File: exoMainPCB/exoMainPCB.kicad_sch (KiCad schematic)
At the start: 76 parts, among them J1 Conn_02x06_Odd_Even, J10 Conn_01x03_Pin, J11 USB_A, J12 USB_A, J13 USB_A, J2 HDMI_A, J3 USB_A, J6 Conn_01x03_Pin, SW3 SW_SPDT, SW4 SW_SPDT, U1 MCP2515-I/ST, U14 SI8642ED-B-IS, U15 SN65HVD230D, U16 SN65HVD230D, U17 SM24CANB-02HTG, U18 SM24CANB-02HTG, U2 MCP2515-I/ST, U3 BNO085, U4 SL2.1A, U5 MCP3008, Y1 16 MHz, Y2 16 MHz, Y3 12 MHz, Y4 32.768 kHz

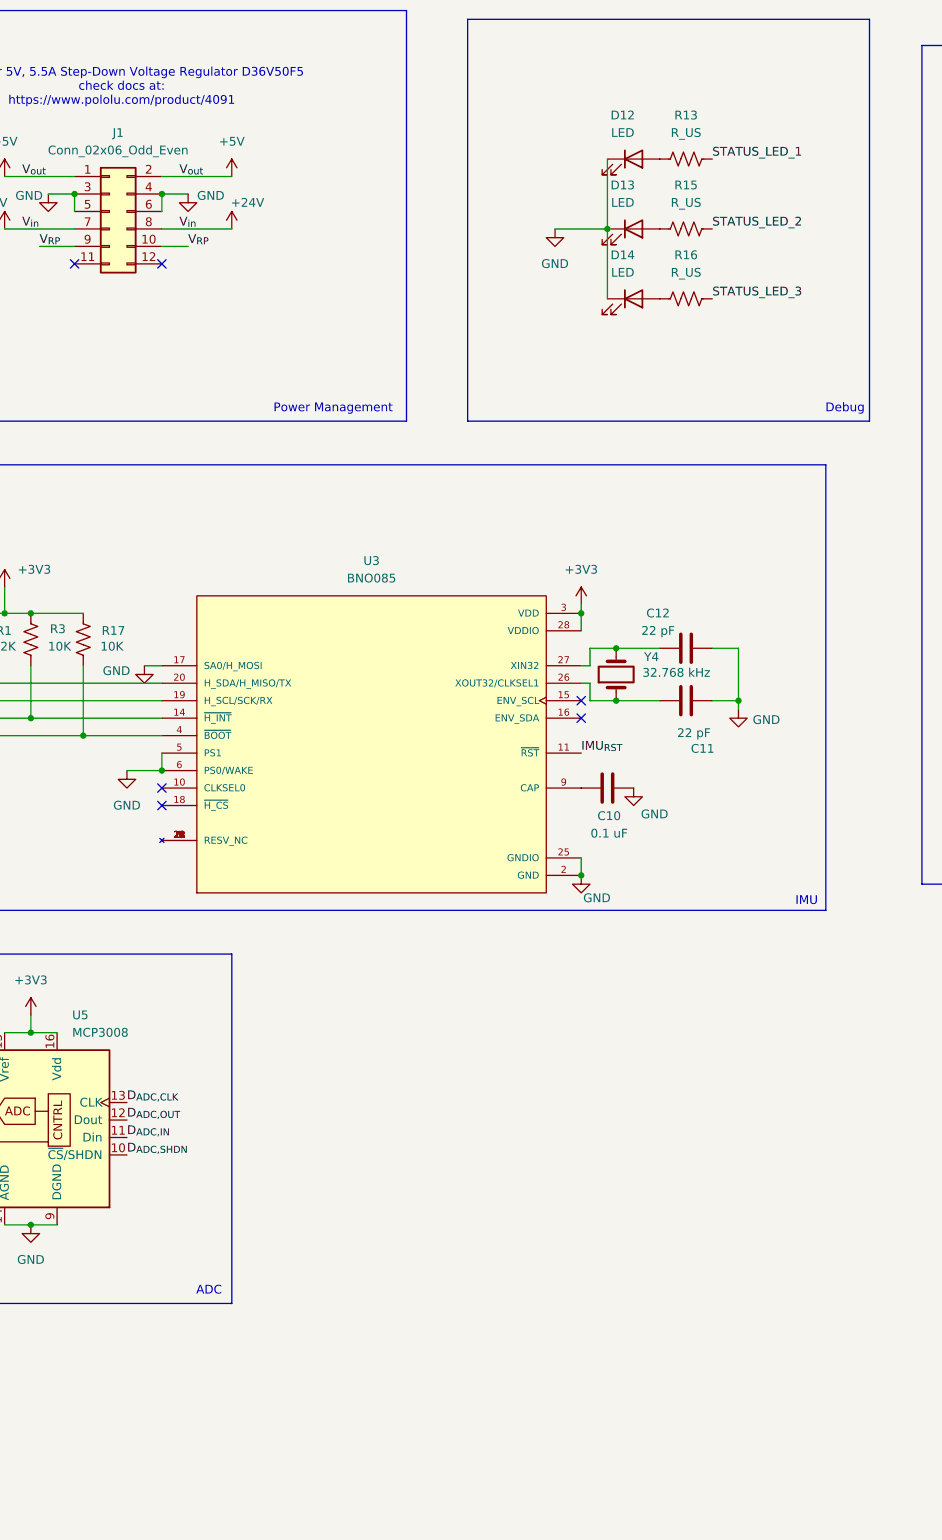
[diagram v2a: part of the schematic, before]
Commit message: added headers to connect to sensors + terminals for battery
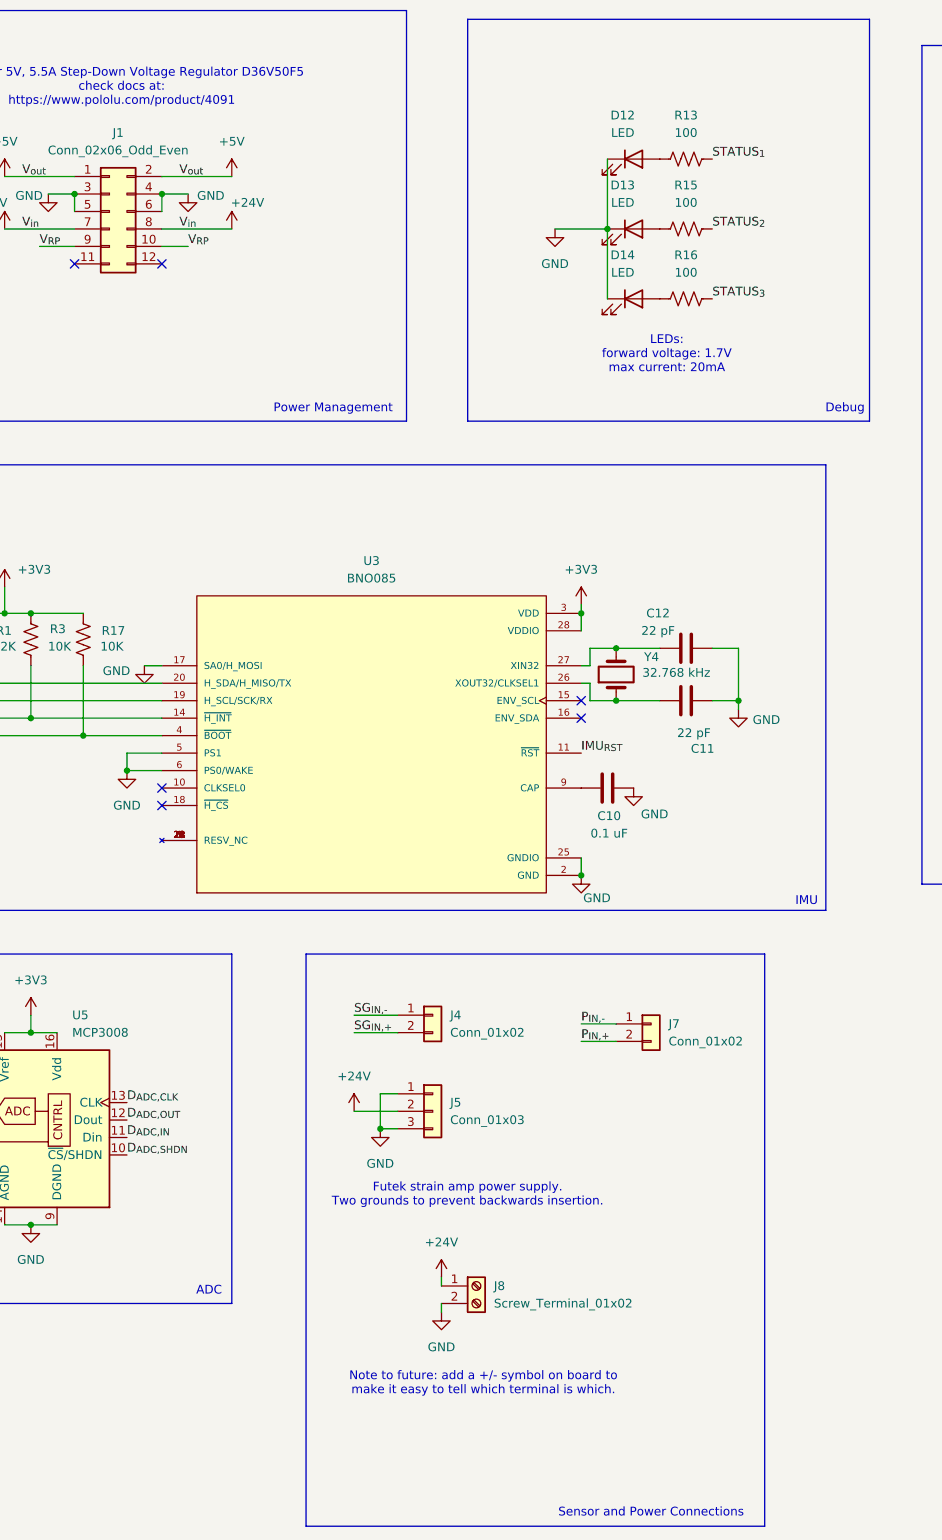
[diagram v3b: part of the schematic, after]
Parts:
- added J4, J7: Conn_01x02, symbol Connector_Generic:Conn_01x02
- added J5: Conn_01x03, symbol Connector_Generic:Conn_01x03
- added J8: Screw_Terminal_01x02, symbol Connector:Screw_Terminal_01x02
- D12, D13, D14: footprint (none) -> LED_SMD:LED_1206_3216Metric
- R13, R15, R16: value R_US -> 100
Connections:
- net +24V: now also J5.2 (Pin_2), J8.1 (Pin_1)
- net GND: now also J5.1 (Pin_1), J5.3 (Pin_3), J8.2 (Pin_2)
- net P_{IN,+}: now also J7.2 (Pin_2)
- net P_{IN,-}: now also J7.1 (Pin_1)
- net SG_{IN,+}: now also J4.2 (Pin_2)
- net SG_{IN,-}: now also J4.1 (Pin_1)
- net STATUS_LED_1 renamed STATUS_{1}
- net STATUS_LED_2 renamed STATUS_{2}
- net STATUS_LED_3 renamed STATUS_{3}
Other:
- note added: "Futek strain amp power supply. Two grounds to prevent backwards insertion."
- note added: "LEDs: forward voltage: 1.7V max current: 20mA"
- note added: "Note to future: add a +/- symbol on board to make it easy to tell which terminal is which."
- note added: "Sensor and Power Connections"

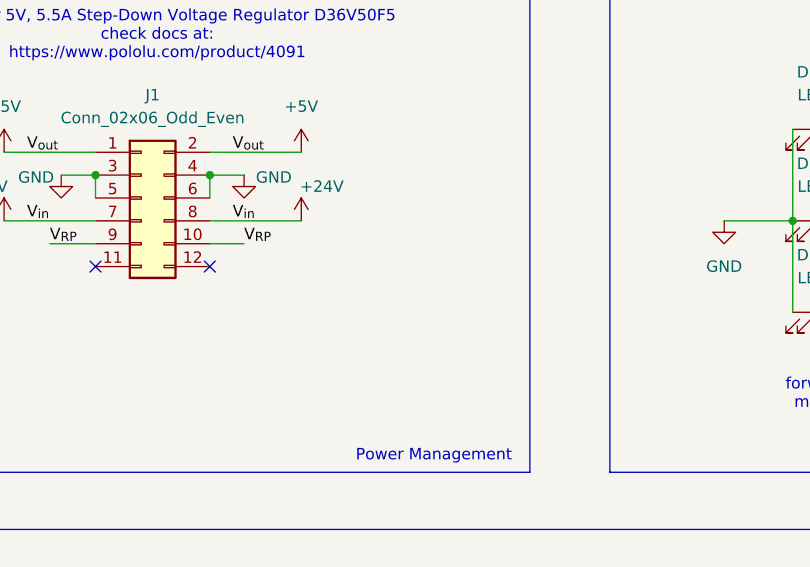
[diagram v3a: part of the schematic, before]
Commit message: added power indicator LED
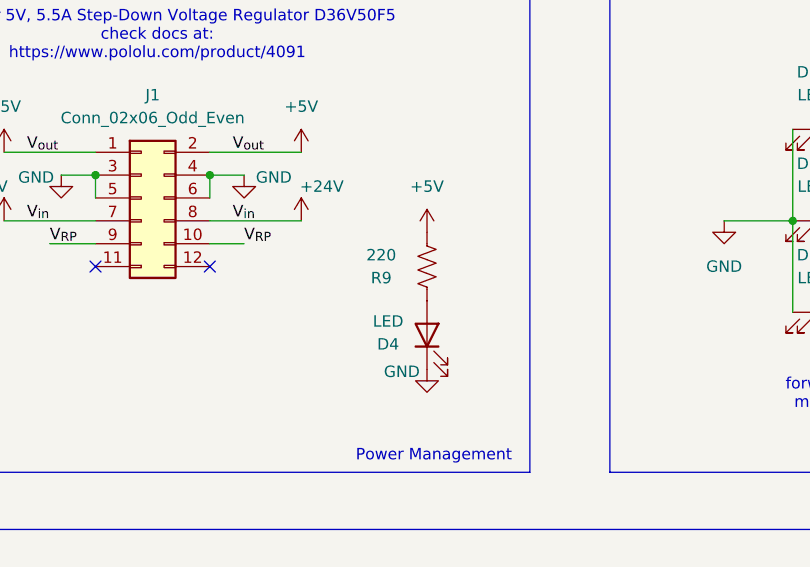
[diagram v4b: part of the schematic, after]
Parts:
- added D4: LED, LED_SMD:LED_1206_3216Metric, symbol Device:LED
- added R9: 220, symbol Device:R_US
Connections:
- net +5V: now also R9.2
- net GND: now also D4.1 (K)
- new net: D4.2 (A), R9.1
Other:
- company: (none) -> Stanford Biomechatronics Lab
- title: (none) -> Untethered Ankle Exoskeleton Control Board

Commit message: added external SD and connected all pins to CM5
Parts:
- added C18: 10uF, symbol Device:C
- added J15: Micro_SD_Card_Det2, symbol Connector:Micro_SD_Card_Det2
- added J9: Screw_Terminal_01x02, symbol Connector:Screw_Terminal_01x02
- added R12: 12K, symbol Device:R_US
- added U6: RT9742GGJ5, Package_TO_SOT_SMD:SOT-23-5, symbol CM5IO:RT9742GGJ5
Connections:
- net D_{ADC,CLK} is gone; now on net SCK: U5.13 (CLK)
- net D_{ADC,IN} is gone; now on net MOSI: U5.11 (Din)
- net D_{ADC,OUT} is gone; now on net MISO: U5.12 (Dout)
- net D_{ADC,SHDN} is gone; now on net D_{CS,ADC}: U5.10 (~{CS}/SHDN)
- net D_{SCK0} is gone; now on net SCK: U1.14 (SCK)
- net D_{SCK1} is gone; now on net SCK: U2.14 (SCK)
- net D_{SI0} is gone; now on net MOSI: U1.16 (SI)
- net D_{SI1} is gone; now on net MOSI: U2.16 (SI)
- net D_{SO0} is gone; now on net MISO: U1.17 (SO)
- net D_{SO1} is gone; now on net MISO: U2.17 (SO)
- net +24V: now also J9.1 (Pin_1)
- net +3V3: now also Module1.78 (GPIO_VREF(1.8v/3.3v_Input)), Module1.84 (+3.3v_(Output)), Module1.86 (+3.3v_(Output)), R12.1, U6.5 (IN)
- net +5V: now also Module1.77 (+5v_(Input)), Module1.79 (+5v_(Input)), Module1.81 (+5v_(Input)), Module1.83 (+5v_(Input)), Module1.85 (+5v_(Input)), Module1.87 (+5v_(Input))
- net D_{CS0}: now also Module1.24 (GPIO26)
- net D_{CS1}: now also Module1.26 (GPIO19)
- net D_{HDMI0_CLK_N}: now also Module1.190 (HDMI0_CLK_N)
- net D_{HDMI0_CLK_P}: now also Module1.188 (HDMI0_CLK_P)
- net D_{HDMI0_HOTPLUG}: now also Module1.153 (HDMI0_HOTPLUG)
- net D_{HDMI0_SCL}: now also Module1.200 (HDMI0_SCL)
- net D_{HDMI0_SDA}: now also Module1.199 (HDMI0_SDA)
- net D_{HDMI0_TX0_N}: now also Module1.184 (HDMI0_TX0_N)
- net D_{HDMI0_TX0_P}: now also Module1.182 (HDMI0_TX0_P)
- net D_{HDMI0_TX1_N}: now also Module1.178 (HDMI0_TX1_N)
- net D_{HDMI0_TX1_P}: now also Module1.176 (HDMI0_TX1_P)
- net D_{HDMI0_TX2_N}: now also Module1.172 (HDMI0_TX2_N)
- net D_{HDMI0_TX2_P}: now also Module1.170 (HDMI0_TX2_P)
- net D_{INT0}: now also Module1.28 (GPIO13)
- net D_{INT1}: now also Module1.30 (GPIO6)
- net D_{USB_N}: now also Module1.103 (USB2_N)
- net D_{USB_P}: now also Module1.105 (USB2_P)
- net GND: now also Module1.1 (GND), Module1.107 (GND), Module1.108 (GND), Module1.113 (GND), Module1.114 (GND), Module1.119 (GND), Module1.120 (GND), Module1.125 (GND), Module1.126 (GND), Module1.13 (GND), Module1.131 (GND), Module1.132 (GND), Module1.137 (GND), Module1.138 (GND), Module1.14 (GND), Module1.144 (GND), Module1.150 (GND), Module1.155 (GND), Module1.156 (GND), Module1.161 (GND), Module1.162 (GND), Module1.167 (GND), Module1.168 (GND), Module1.173 (GND), Module1.174 (GND), Module1.179 (GND), Module1.180 (GND), Module1.185 (GND), Module1.186 (GND), Module1.191 (GND), Module1.192 (GND), Module1.197 (GND), Module1.198 (GND), Module1.2 (GND), Module1.22 (GND), Module1.23 (GND), Module1.32 (GND), Module1.33 (GND), Module1.42 (GND), Module1.43 (GND), Module1.52 (GND), Module1.53 (GND), Module1.59 (GND), Module1.60 (GND), Module1.65 (GND), Module1.66 (GND), Module1.7 (GND), Module1.71 (GND), Module1.74 (GND), Module1.8 (GND), Module1.98 (GND), C18.2, J15.11 (SHIELD), J15.6 (VSS), J9.2 (Pin_2), U6.2 (GND)
- net IMU_{BOOT}: now also Module1.46 (GPIO22)
- net IMU_{HINT}: now also Module1.48 (GPIO27)
- net IMU_{RST}: now also Module1.50 (GPIO17)
- net SCL: now also Module1.56 (GPIO3)
- net SDA: now also Module1.58 (GPIO2)
- net STATUS_{1}: now also Module1.41 (GPIO25)
- net STATUS_{2}: now also Module1.39 (GPIO8)
- net STATUS_{3}: now also Module1.37 (GPIO7)
- net D_{CS,ADC}: now reaches Module1.34 (GPIO5)
- net SCK: now reaches Module1.38 (GPIO11)
- net MISO: now reaches Module1.40 (GPIO9)
- net MOSI: now reaches Module1.44 (GPIO10)
- net SD_{CLK}: now reaches Module1.57 (SD_CLK)
- net SD_{CLK}: now also J15.5 (CLK)
- net SD_{DAT,3}: now reaches Module1.61 (SD_DAT3)
- net SD_{DAT,3}: now also J15.2 (DAT3/CD)
- net SD_{CMD}: now reaches Module1.62 (SD_CMD)
- net SD_{CMD}: now also J15.3 (CMD)
- net SD_{DAT,0}: now reaches Module1.63 (SD_DAT0)
- net SD_{DAT,0}: now also J15.7 (DAT0)
- net SD_{DAT,1}: now reaches Module1.67 (SD_DAT1)
- net SD_{DAT,1}: now also J15.8 (DAT1)
- net SD_{DAT,2}: now reaches Module1.69 (SD_DAT2)
- net SD_{DAT,2}: now also J15.1 (DAT2)
- net SD_{PWRON}: now reaches Module1.75 (SD_PWR_ON)
- net SD_{PWRON}: now also R12.2, U6.4 (EN)
- new net SD_{PWR}: C18.1, J15.4 (VDD), U6.1 (OUT)
- no-connect marks 31 -> 32

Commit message: \added voltage inputs for the USB hub and CAN, down to 2 errors (can explain possible fix), 12 warnings (ignore the units warnings for the diode for now)
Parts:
- removed C34: 104, symbol Device:C
- removed R27: 120, symbol Device:R_US
- removed SW4: SW_SPDT, symbol Switch:SW_SPDT
- removed U16: SN65HVD230D, SOIC127P600X175-8N, symbol SN65HVD230:SN65HVD230D
- removed U18: SM24CANB-02HTG, SM24CANB02HTG, symbol SM24CANB:SM24CANB-02HTG
- added C19: 104, symbol Device:C
- added R14: 120, symbol Device:R_US
- added SW1: SW_SPDT, symbol Switch:SW_SPDT
- added U7: SN65HVD230D, SOIC127P600X175-8N, symbol SN65HVD230:SN65HVD230D
- added U8: SM24CANB-02HTG, SM24CANB02HTG, symbol SM24CANB:SM24CANB-02HTG
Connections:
- net +3V3: now also C16.2, C33.2, C5.2, C6.1, R4.1, R5.1, U1.20 (VDD), U14.1 (VDD1), U14.16 (VDD2), U15.3 (VCC), U2.20 (VDD), U4.13 (VDD33), C19.2, U7.3 (VCC)
- net D_{HDMI0_CEC}: now also Module1.151 (HDMI0_CEC)
- net GNDS: now also C33.1, R6.2, R7.2, C19.1, U7.2 (GND), U8.3; no longer C33.2, R6.1, R7.1
- net RXD_1B: now also U7.4 (R)
- net TXD_1B: now also U7.1 (D)
- net at J10.3 (Pin_3): now also R14.2, U7.7 (CANH), U8.1
- net +1V8: now reaches C15.2, U4.14 (VDD18)
- net +1V8: now also Module1.88 (+1.8v_(Output))
- net at J10.2 (Pin_2): now also SW1.1 (A), U7.6 (CANL), U8.2
- net at U15.8 (RS): now also R6.1; no longer R6.2
- new net: R7.1, U7.8 (RS)
- new net: R14.1, SW1.2 (B)
- no-connect marks 32 -> 143
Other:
- moved on the sheet: C33, C5, C6, R26, R6, SW3, U17

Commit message: removed sd card due to emmc, added battery voltage connection to ADC
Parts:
- removed C18: 10uF, symbol Device:C
- removed J15: Micro_SD_Card_Det2, symbol Connector:Micro_SD_Card_Det2
- removed U6: RT9742GGJ5, Package_TO_SOT_SMD:SOT-23-5, symbol CM5IO:RT9742GGJ5
- added J14: Screw_Terminal_01x02, symbol Connector:Screw_Terminal_01x02
- added R18: 100k, symbol Device:R_US
- added SW2: SW_Push, symbol Switch:SW_Push
- R12: value 12K -> 900k
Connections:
- net +24V: now also R12.2, J14.1 (Pin_1)
- net +3V3: no longer R12.1
- net GND: now also U5.6 (CH5), J14.2 (Pin_2), R18.1, SW2.2
- net at Module1.92 (PWR_BUT): now also SW2.1
- net V_{battery}: now reaches U5.5 (CH4)
- net V_{battery}: now also R12.1, R18.2
- net SD_{CLK}: no longer names the net of Module1.57 (SD_CLK)
- net SD_{CMD}: no longer names the net of Module1.62 (SD_CMD)
- net SD_{DAT,0}: no longer names the net of Module1.63 (SD_DAT0)
- net SD_{DAT,1}: no longer names the net of Module1.67 (SD_DAT1)
- net SD_{DAT,2}: no longer names the net of Module1.69 (SD_DAT2)
- net SD_{DAT,3}: no longer names the net of Module1.61 (SD_DAT3)
- net SD_{PWRON}: no longer names the net of Module1.75 (SD_PWR_ON)
- net SD_{PWRON}: no longer R12.2
- no-connect marks 143 -> 144
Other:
- moved on the sheet: D4, J1, J8, R9

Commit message: added solder bridges, resolved errors
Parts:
- removed J9: Screw_Terminal_01x02, symbol Connector:Screw_Terminal_01x02
- added JP3, JP4, JP5, JP6, JP9: SolderJumper_2_Bridged, symbol Jumper:SolderJumper_2_Bridged
- R12: value 900k -> 90k
- R18: value 100k -> 10k
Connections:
- net +3V3: now also JP3.2 (B), JP4.2 (B), JP5.2 (B), JP9.2 (B); no longer C19.2, C33.2, C5.2, C6.1, Module1.78 (GPIO_VREF(1.8v/3.3v_Input)), Module1.84 (+3.3v_(Output)), Module1.86 (+3.3v_(Output)), R4.1, R5.1, U1.20 (VDD), U14.1 (VDD1), U14.16 (VDD2), U15.3 (VCC), U2.20 (VDD), U3.28 (VDDIO), U3.3 (VDD), U5.15 (Vref), U5.16 (Vdd), U7.3 (VCC)
- net +5V: now also JP6.1 (A); no longer Module1.77 (+5v_(Input)), Module1.79 (+5v_(Input)), Module1.81 (+5v_(Input)), Module1.83 (+5v_(Input)), Module1.85 (+5v_(Input)), Module1.87 (+5v_(Input))
- new net: JP3.1 (A), U3.28 (VDDIO), U3.3 (VDD)
- new net: JP6.2 (B), Module1.77 (+5v_(Input)), Module1.79 (+5v_(Input)), Module1.81 (+5v_(Input)), Module1.83 (+5v_(Input)), Module1.85 (+5v_(Input)), Module1.87 (+5v_(Input))
- new net: JP9.1 (A), Module1.78 (GPIO_VREF(1.8v/3.3v_Input)), Module1.84 (+3.3v_(Output)), Module1.86 (+3.3v_(Output))
- new net: JP4.1 (A), U5.15 (Vref), U5.16 (Vdd)
- new net +3V3_{CAN}: C19.2, C33.2, C5.2, C6.1, JP5.1 (A), R4.1, R5.1, U1.20 (VDD), U14.1 (VDD1), U14.16 (VDD2), U15.3 (VCC), U2.20 (VDD), U7.3 (VCC)
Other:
- moved on the sheet: U5
